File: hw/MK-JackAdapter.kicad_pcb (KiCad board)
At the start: 2 copper layers, 25.4 x 30.5 mm, 3 parts, among them J1 KEY-PADDLE-4, J2 KEY-PADDLE-8

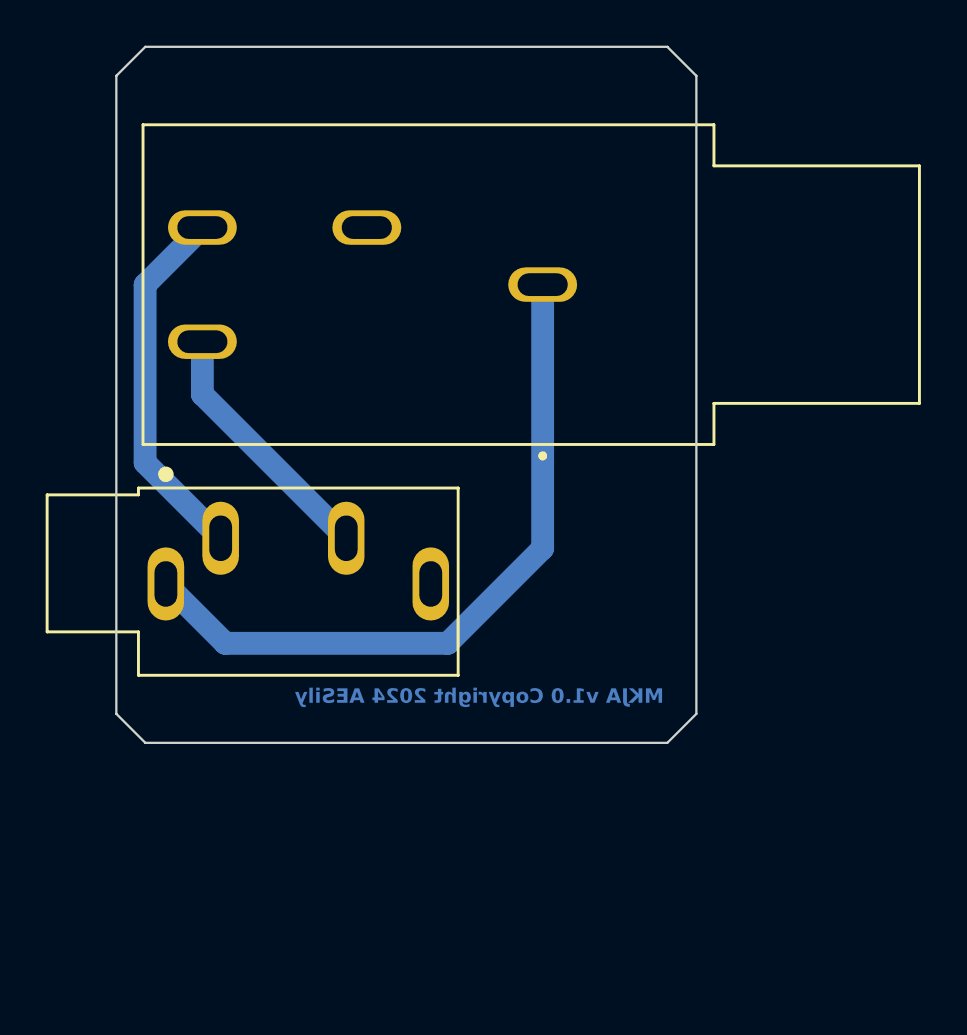
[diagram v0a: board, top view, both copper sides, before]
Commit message: KSInf-MkIII: New  JA: Add terminal block
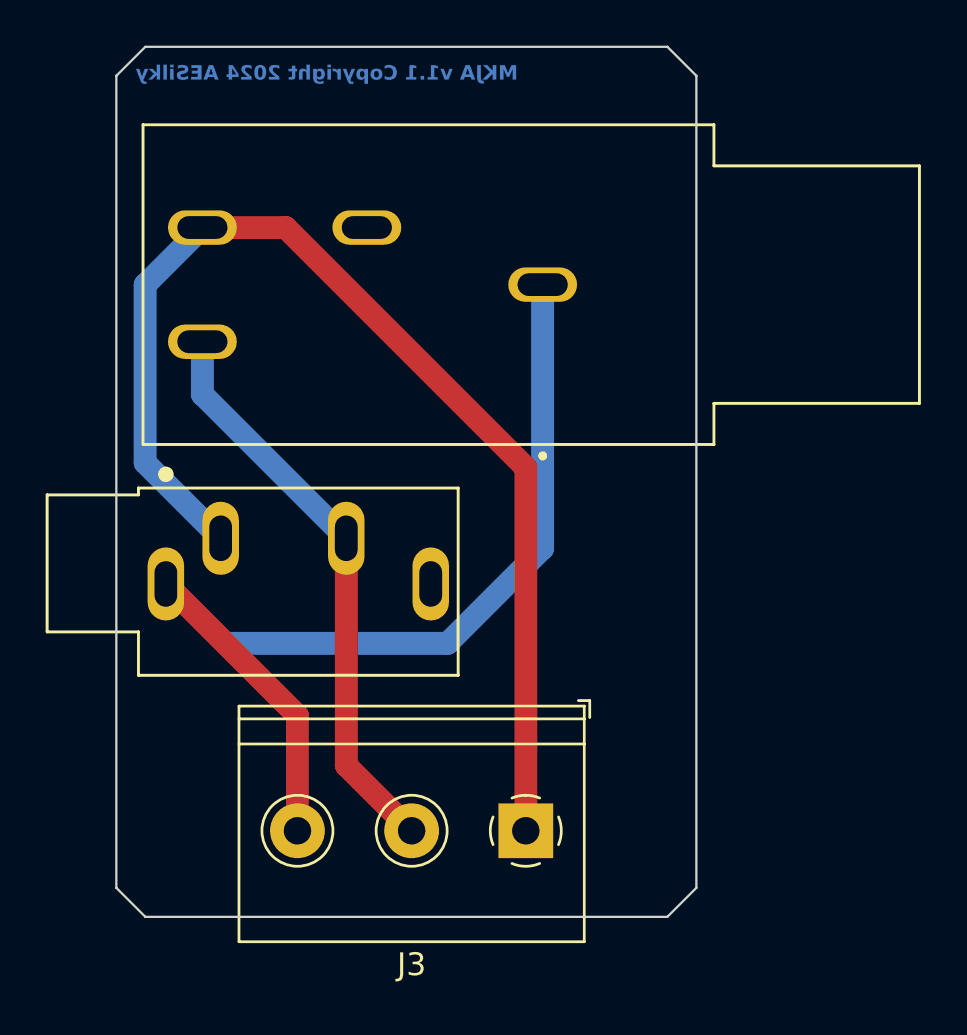
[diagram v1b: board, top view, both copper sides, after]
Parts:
- added J3: Screw_Terminal_01x03, TerminalBlock_Philmore:TerminalBlock_Philmore_TB133_1x03_P5.00mm_Horizontal, F.Cu at (119.3, 127.4)
- moved G*** 10.4 mm to (123.6, 100.7)
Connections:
- net Net-(J1-Pad1) renamed /COMMON
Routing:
- net /KEY_PDL_DOT-: track 16.0 -> 50.4 mm
- net /PDL_DASH-: track 11.2 -> 25.2 mm
- net /COMMON: track 30.9 -> 44.0 mm
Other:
- board size 25.4 x 30.5 mm -> 25.4 x 38.1 mm
- board text added: "CMN"
- board text added: "DASH"
- board text added: "KEY DOT"
- board text added: "MKJA v1.1 Copyright 2024 AESilky"
- board text added: "R"
- board text added: "S"
- board text added: "T"
- board text removed: "MKJA v1.0 Copyright 2024 AESily"
